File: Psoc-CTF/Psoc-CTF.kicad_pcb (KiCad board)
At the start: 2 copper layers, 100 x 80 mm, 86 parts, among them IC1 CY8C4248LQI-BL583, J1 Conn_01x02, J2 Conn_01x03, J3 Prog, J4 Conn_01x04, J5 USB3076-XX-X_REVC, P1 Power, P2 Analog, P3 Digital, P4 Digital, P5 CONN_01X01, P6 CONN_01X01, P7 CONN_01X01, P8 CONN_01X01, SW1 FSM4JSMATR, SW2 FSM4JSMATR, U1 AMS1117-5.0, U2 AMS1117-3.3, U3 ESP32-WROOM-32D, U4 FM24C04B-GTR, U5 CY7C65211-24LTXI, Y1 24MHz, Y2 32.768Khz

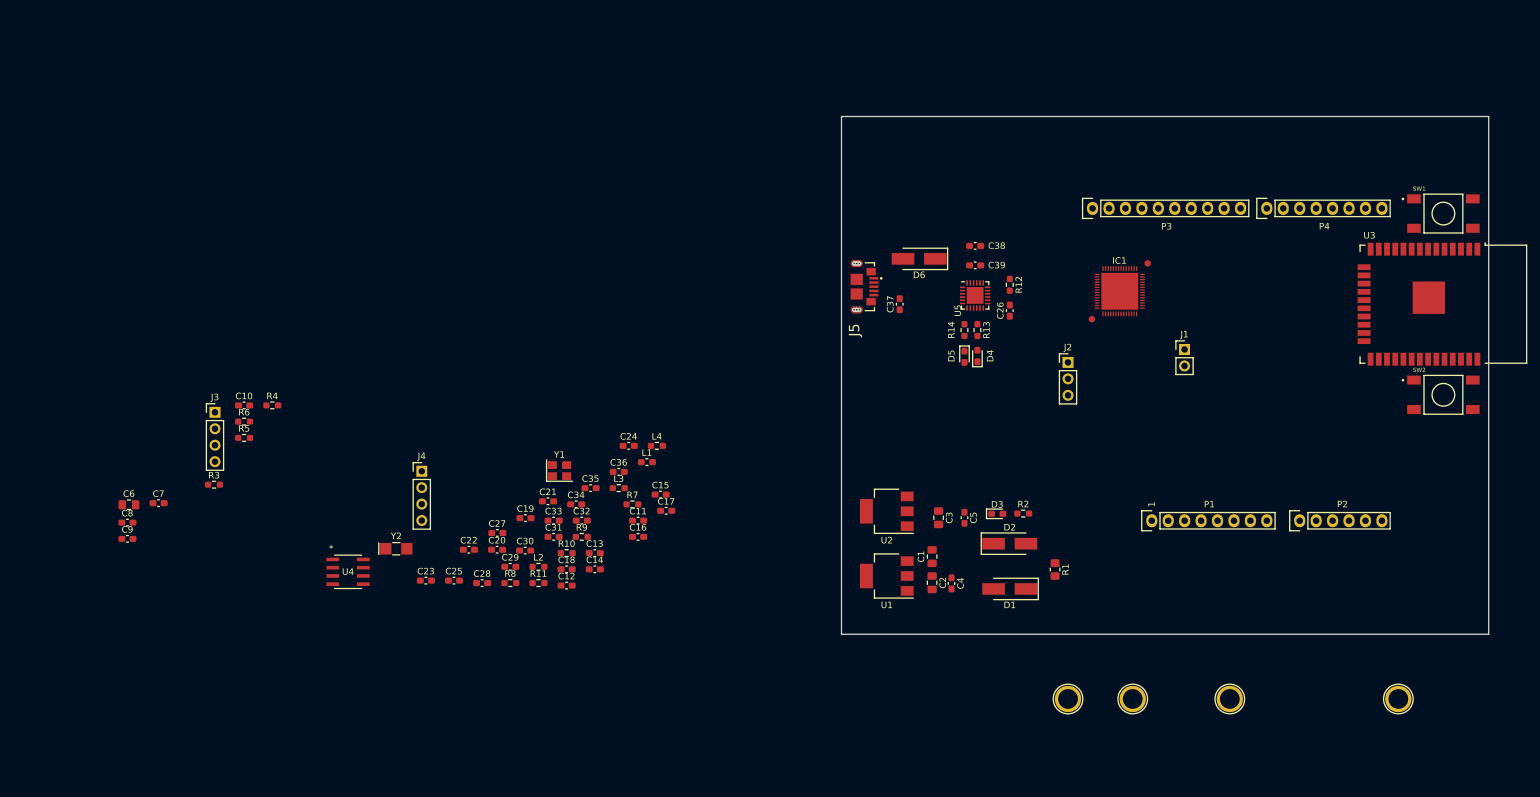
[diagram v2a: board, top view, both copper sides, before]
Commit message: anexo slider y led rgb
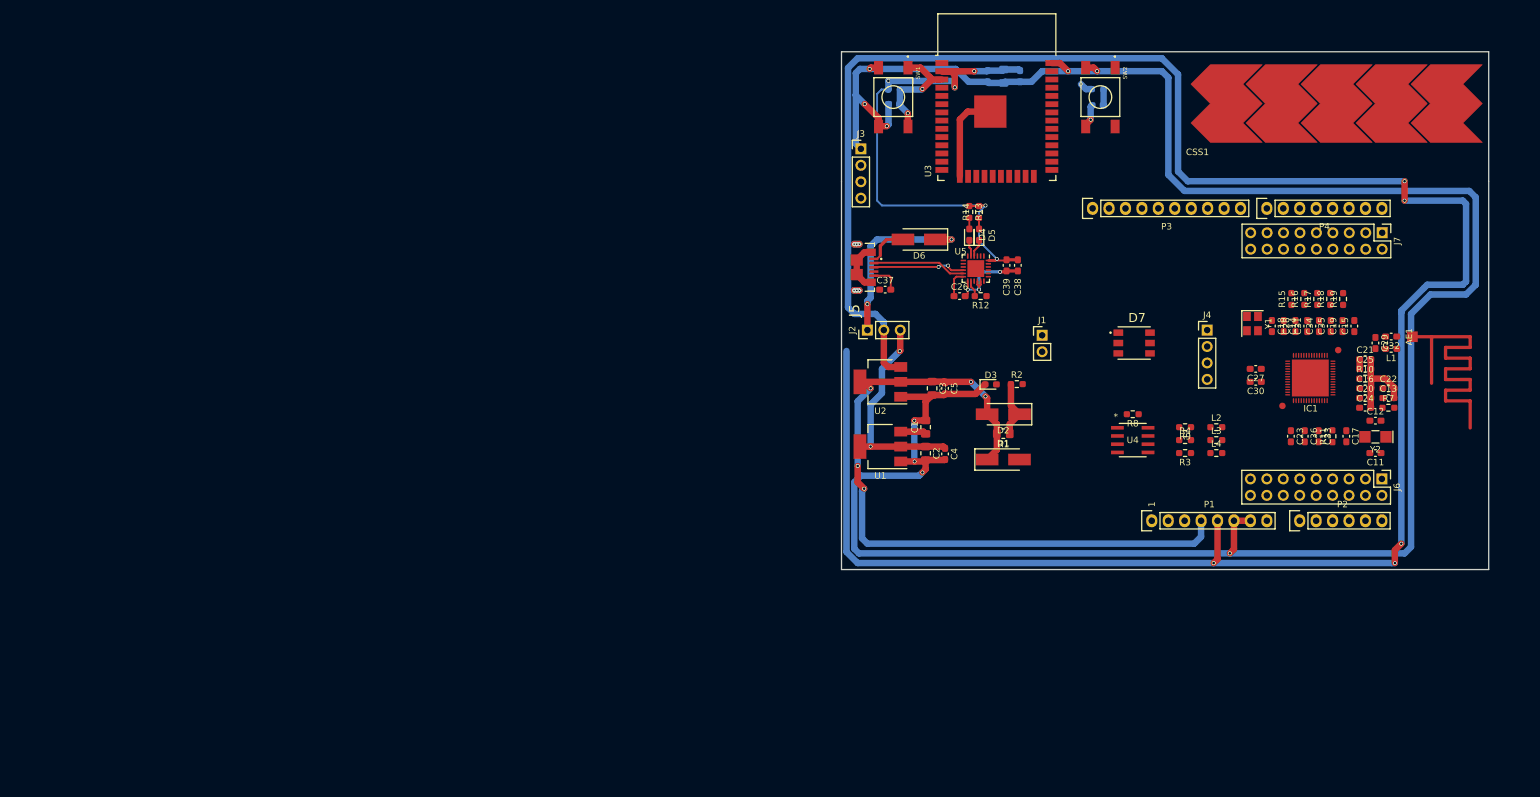
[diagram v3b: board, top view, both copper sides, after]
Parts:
- removed P5, P6, P7, P8: CONN_01X01, Socket_Arduino_Uno:Arduino_1pin
- added AE1: Antenna_Shield, Psoc-CTF:Antena_pad, F.Cu at (199.2, 90.4)
- added CSS1: cap_slider, Psoc-CTF:CAP_SLIDER_5_PADS, F.Cu at (210.0, 48.4)
- added D7: COM-11821, Psoc-CTF:LED_COM-11821, F.Cu at (156.2, 91.4)
- added J6: Header 9x2, Connector_PinHeader_2.54mm:PinHeader_2x09_P2.54mm_Vertical, F.Cu at (194.5, 112.4)
- added J7: Header 9x2, Connector_PinHeader_2.54mm:PinHeader_2x09_P2.54mm_Vertical, F.Cu at (194.5, 74.3)
- added R15: 560, Resistor_SMD:R_0603_1608Metric_Pad0.98x0.95mm_HandSolder, F.Cu at (180.5, 84.6)
- added R16: 560, Resistor_SMD:R_0603_1608Metric_Pad0.98x0.95mm_HandSolder, F.Cu at (182.5, 84.6)
- added R17: 560, Resistor_SMD:R_0603_1608Metric_Pad0.98x0.95mm_HandSolder, F.Cu at (184.5, 84.6)
- added R18: 560, Resistor_SMD:R_0603_1608Metric_Pad0.98x0.95mm_HandSolder, F.Cu at (186.5, 84.6)
- added R19: 560, Resistor_SMD:R_0603_1608Metric_Pad0.98x0.95mm_HandSolder, F.Cu at (188.5, 84.6)
- C10, C6, C7, C8, C9, R5, R6: moved to B.Cu
- moved C8 154.2 mm to (138.6, 50.1), turned to 270 degrees
- moved Y2 152.3 mm to (193.5, 105.9), turned to 180 degrees
- moved C6 150.5 mm to (136.1, 50.1), turned to 270 degrees
- moved R3 150.1 mm to (164.1, 108.4), turned to 180 degrees
- moved C25 144.5 mm to (191.9, 95.4)
- moved C22 144.2 mm to (195.5, 98.4)
- moved C7 144.1 mm to (133.6, 50.1), turned to 270 degrees
- moved R6 141.5 mm to (150.6, 52.1)
- moved R4 141.1 mm to (164.1, 106.4)
- moved C10 139.8 mm to (150.6, 54.6), turned to 180 degrees
- moved C29 138.1 mm to (193.5, 91.4), turned to 270 degrees
- moved C9 136.2 mm to (119.1, 54.4), turned to 180 degrees
- moved C20 136.2 mm to (191.9, 99.9)
- moved C23 135.5 mm to (180.4, 105.8), turned to 270 degrees
- moved C28 131.8 mm to (181.1, 88.7), turned to 90 degrees
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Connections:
- net /MCU_Target/0(Rx) renamed P1.4
- net /MCU_Target/1(Tx) renamed P1.5
- net /MCU_Target/P4.0 renamed P4.0
- net /MCU_Target/P4.1 renamed P4.1
- net /MCU_Target/SWCLK renamed P0.7
- net /MCU_Target/SWDIO renamed P0.6
- net /MCU_Target/T_MCU_SCL renamed P3.5
- net /MCU_Target/T_MCU_SDA renamed P3.4
- IC1 pad 11: Net-(IC1-Pad11) -> GND
- IC1 pad 13: Net-(IC1-Pad13) -> GND
- IC1 pad 19: /MCU_Target/11(**/MOSI) -> P0.0
- IC1 pad 20: /MCU_Target/12(MISO) -> P0.1
- IC1 pad 21: /MCU_Target/10(**/SS) -> P0.2
- IC1 pad 22: /MCU_Target/13(SCK) -> P0.3
- IC1 pad 24: /MCU_Target/9(**) -> P0.4
- IC1 pad 25: /MCU_Target/8 -> P0.5
- IC1 pad 28: /MCU_Target/7 -> P1.0
- IC1 pad 29: /MCU_Target/6(**) -> P1.1
- IC1 pad 30: /MCU_Target/5(**) -> P1.2
- IC1 pad 31: /MCU_Target/4 -> P1.3
- IC1 pad 34: /MCU_Target/2 -> P1.6
- IC1 pad 35: /MCU_Target/3(**) -> P1.7
- IC1 pad 37: Net-(IC1-Pad37) -> P2.0
- IC1 pad 38: Net-(IC1-Pad38) -> P2.1
- IC1 pad 39: Net-(IC1-Pad39) -> P2.2
- IC1 pad 40: Net-(IC1-Pad40) -> P2.3
- IC1 pad 41: Net-(IC1-Pad41) -> P2.4
- IC1 pad 42: Net-(IC1-Pad42) -> P2.5
- IC1 pad 43: Net-(IC1-Pad43) -> P2.6
- IC1 pad 44: Net-(IC1-Pad44) -> P2.7
- IC1 pad 47: /MCU_Target/A0 -> P3.0
- IC1 pad 48: /MCU_Target/A1 -> P3.1
- IC1 pad 49: /MCU_Target/A2 -> P3.2
- IC1 pad 50: /MCU_Target/A3 -> P3.3
- IC1 pad 53: Net-(IC1-Pad53) -> P3.6
- IC1 pad 54: Net-(IC1-Pad54) -> P3.7
- IC1 pad 57: /MCU_Target/AMP_READ -> GND
- IC1 pad 7: Net-(IC1-Pad7) -> P5.0
- IC1 pad 8: Net-(IC1-Pad8) -> P5.1
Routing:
- net GND: track 0.00 -> 460.6 mm, vias 0 -> 13
- net +5V: track 0.00 -> 355.2 mm, vias 0 -> 5
- net +3V3: track 0.00 -> 113.8 mm, vias 0 -> 5
- net VDD: track 0.00 -> 93.6 mm, vias 0 -> 6
- net /power_supply/5VExt: track 0.00 -> 33.2 mm, vias 0 -> 2
- net /MCU_Target/5VBUS: track 0.00 -> 28.6 mm, vias 0 -> 2
- net /MONITOR/EN: track 0.00 -> 17.6 mm, vias 0 -> 2
- net /MCU_Target/D-: track 0.00 -> 14.5 mm
- net /MCU_Target/D+: track 0.00 -> 14.3 mm, vias 0 -> 2
- net GNDPWR: track 0.00 -> 7.70 mm
- net Net-(D6-Pad2): track 0.00 -> 6.62 mm
- net Net-(C26-Pad1): track 0.00 -> 4.21 mm
- net +12V: track 0.00 -> 3.99 mm
- net Net-(D5-Pad1): track 0.00 -> 2.75 mm
- net Net-(R12-Pad2): track 0.00 -> 2.56 mm
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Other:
- outline, holes or cut-outs redrawn

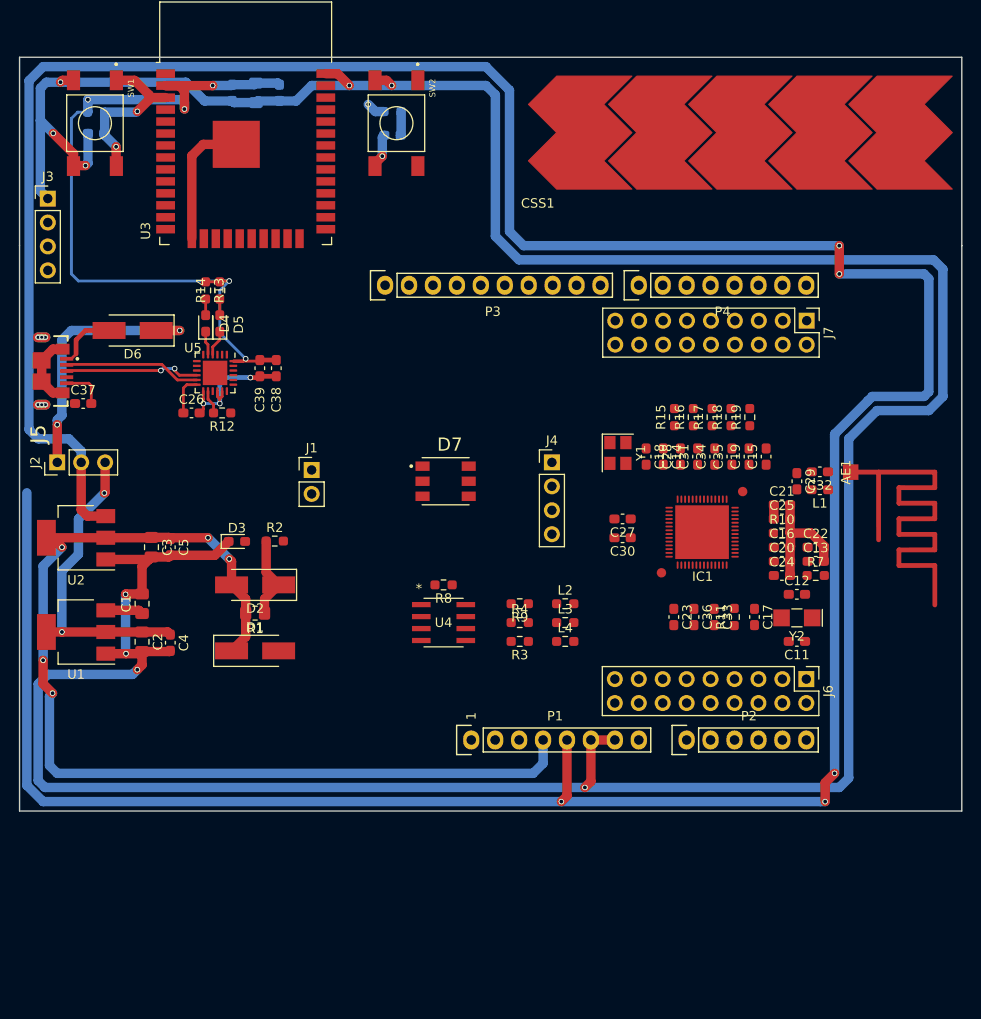
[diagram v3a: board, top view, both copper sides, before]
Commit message: Anexo de nuevos pulsadores y arreglo de resistencias
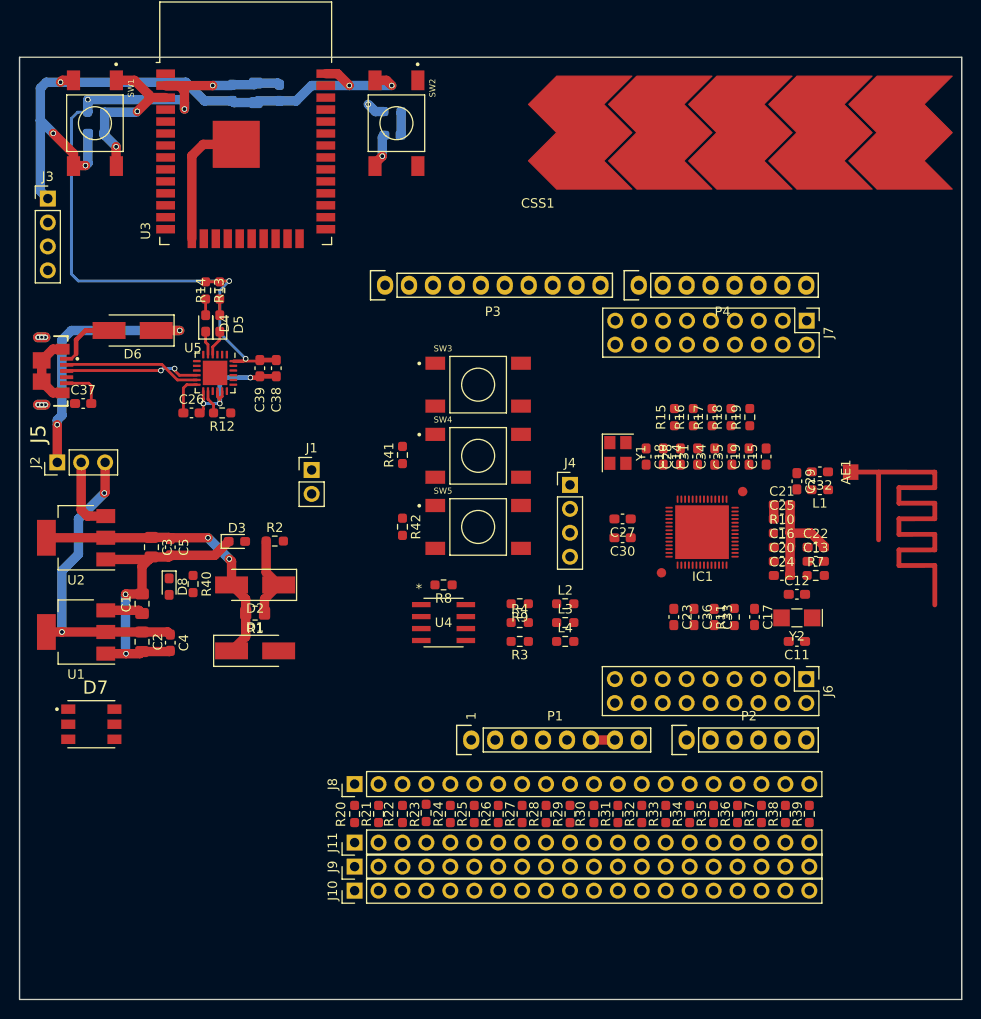
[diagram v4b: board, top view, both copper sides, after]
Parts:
- added D8: LED, LED_SMD:LED_0603_1608Metric_Pad1.05x0.95mm_HandSolder, F.Cu at (126.9, 102.5)
- added J10: Conn_01x20, Connector_PinHeader_2.54mm:PinHeader_1x20_P2.54mm_Vertical, F.Cu at (146.6, 134.8)
- added J11: Conn_01x20, Connector_PinHeader_2.54mm:PinHeader_1x20_P2.54mm_Vertical, F.Cu at (146.6, 129.7)
- added J8: Conn_01x20, Connector_PinHeader_2.54mm:PinHeader_1x20_P2.54mm_Vertical, F.Cu at (146.6, 123.5)
- added J9: Conn_01x20, Connector_PinHeader_2.54mm:PinHeader_1x20_P2.54mm_Vertical, F.Cu at (146.6, 132.3)
- added R20: 1K, Resistor_SMD:R_0603_1608Metric_Pad0.98x0.95mm_HandSolder, F.Cu at (146.6, 126.7)
- added R21: 1K5, Resistor_SMD:R_0603_1608Metric_Pad0.98x0.95mm_HandSolder, F.Cu at (149.1, 126.7)
- added R22: 2K2, Resistor_SMD:R_0603_1608Metric_Pad0.98x0.95mm_HandSolder, F.Cu at (151.6, 126.7)
- added R23: 2K7, Resistor_SMD:R_0603_1608Metric_Pad0.98x0.95mm_HandSolder, F.Cu at (154.1, 126.6)
- added R24: 3K3, Resistor_SMD:R_0603_1608Metric_Pad0.98x0.95mm_HandSolder, F.Cu at (156.7, 126.7)
- added R25: 4K7, Resistor_SMD:R_0603_1608Metric_Pad0.98x0.95mm_HandSolder, F.Cu at (159.3, 126.7)
- added R26: 5K1, Resistor_SMD:R_0603_1608Metric_Pad0.98x0.95mm_HandSolder, F.Cu at (161.8, 126.7)
- added R27: 5K6, Resistor_SMD:R_0603_1608Metric_Pad0.98x0.95mm_HandSolder, F.Cu at (164.3, 126.7)
- added R28: 6K8, Resistor_SMD:R_0603_1608Metric_Pad0.98x0.95mm_HandSolder, F.Cu at (166.9, 126.7)
- added R29: 8K2, Resistor_SMD:R_0603_1608Metric_Pad0.98x0.95mm_HandSolder, F.Cu at (169.4, 126.7)
- added R30: 10K, Resistor_SMD:R_0603_1608Metric_Pad0.98x0.95mm_HandSolder, F.Cu at (172.0, 126.7)
- added R31: 15K, Resistor_SMD:R_0603_1608Metric_Pad0.98x0.95mm_HandSolder, F.Cu at (174.5, 126.7)
- added R32: 22K, Resistor_SMD:R_0603_1608Metric_Pad0.98x0.95mm_HandSolder, F.Cu at (177.0, 126.7)
- added R33: 27K, Resistor_SMD:R_0603_1608Metric_Pad0.98x0.95mm_HandSolder, F.Cu at (179.6, 126.7)
- added R34: 33K, Resistor_SMD:R_0603_1608Metric_Pad0.98x0.95mm_HandSolder, F.Cu at (182.1, 126.7)
- added R35: 47K, Resistor_SMD:R_0603_1608Metric_Pad0.98x0.95mm_HandSolder, F.Cu at (184.7, 126.7)
- added R36: 51K, Resistor_SMD:R_0603_1608Metric_Pad0.98x0.95mm_HandSolder, F.Cu at (187.2, 126.7)
- added R37: 56K, Resistor_SMD:R_0603_1608Metric_Pad0.98x0.95mm_HandSolder, F.Cu at (189.7, 126.7)
- added R38: 68K, Resistor_SMD:R_0603_1608Metric_Pad0.98x0.95mm_HandSolder, F.Cu at (192.3, 126.7)
- added R39: 82K, Resistor_SMD:R_0603_1608Metric_Pad0.98x0.95mm_HandSolder, F.Cu at (194.8, 126.7)
- added R40: 1K, Resistor_SMD:R_0603_1608Metric_Pad0.98x0.95mm_HandSolder, F.Cu at (129.4, 102.3)
- added R41: 10K, Resistor_SMD:R_0603_1608Metric_Pad0.98x0.95mm_HandSolder, F.Cu at (151.6, 88.6)
- added R42: 10K, Resistor_SMD:R_0603_1608Metric_Pad0.98x0.95mm_HandSolder, F.Cu at (151.6, 96.2)
- added SW3: FSM4JSMATR, Psoc-CTF:Push_button_FSM4JSMATR, F.Cu at (159.7, 81.1)
- added SW4: FSM4JSMATR, Psoc-CTF:Push_button_FSM4JSMATR, F.Cu at (159.7, 88.7)
- added SW5: FSM4JSMATR, Psoc-CTF:Push_button_FSM4JSMATR, F.Cu at (159.7, 96.2)
- moved D7 45.6 mm to (118.6, 117.2)
- moved J4 3.07 mm to (169.4, 91.8)
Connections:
- IC1 pad 11: GND -> GND1
- IC1 pad 13: GND -> GND1
- IC1 pad 55: /MCU_Target/AMP_READ -> GND1
- IC1 pad 57: GND -> GND1
- J1 pad 2: /MCU_Target/AMP_READ -> GND1
- U5 pad 1: P1.4 -> P1.5
- U5 pad 23: P1.5 -> P1.4
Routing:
- net +5V: track 355.2 -> 7.92 mm, vias 5 -> 0
- net GND: track 460.6 -> 206.8 mm, vias 13 -> 11
- net +3V3: track 113.8 -> 31.6 mm, vias 5 -> 2
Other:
- board size 100 x 80 mm -> 100 x 100 mm
